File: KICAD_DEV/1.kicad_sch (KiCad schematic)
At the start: 0 parts

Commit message: wired my TMC2209 :D
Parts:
- added C18: 220uF, symbol Device:C
- added C19: 0.1uF, Capacitor_SMD:C_0805_2012Metric, symbol Device:C
- added C20: 0.1uF, symbol Device:C
- added J3, J4: Conn_01x08, symbol Connector_Generic:Conn_01x08
- added J5: Conn_01x02, symbol Connector_Generic:Conn_01x02
- added J6: Conn_01x04, symbol Connector_Generic:Conn_01x04
- added R10, R7, R8, R9: 10K, symbol Device:R
- added R5, R6: 1K, symbol Device:R
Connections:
- new net: J3.7 (Pin_7), R9.1
- new net: J3.5 (Pin_5), R7.1
- new net: J3.6 (Pin_6), R8.1
- new net: J4.3 (Pin_3), J6.4 (Pin_4)
- new net: J4.4 (Pin_4), J6.3 (Pin_3)
- new net: J4.5 (Pin_5), J6.2 (Pin_2)
- new net: J4.6 (Pin_6), J6.1 (Pin_1)
- new net: J3.4 (Pin_4), R5.1, R6.2
- new net +12V: C18.1, C19.1, J4.8 (Pin_8)
- new net +3V3: C20.1, J4.2 (Pin_2), R10.1
- new net GND: C18.2, C19.2, C20.2, J4.1 (Pin_1), J4.7 (Pin_7), R7.2, R8.2, R9.2
- new net TMC2209_DIAG: J5.1 (Pin_1)
- new net TMC2209_DIR: J3.1 (Pin_1)
- new net TMC2209_EN: J3.8 (Pin_8), R10.2
- new net TMC2209_INDEX: J5.2 (Pin_2)
- new net TMC2209_RX: R5.2
- new net TMC2209_STEP: J3.2 (Pin_2)
- new net TMC2209_TX: R6.1
- no-connect marks 0 -> 1
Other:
- note added: "TMC2209"

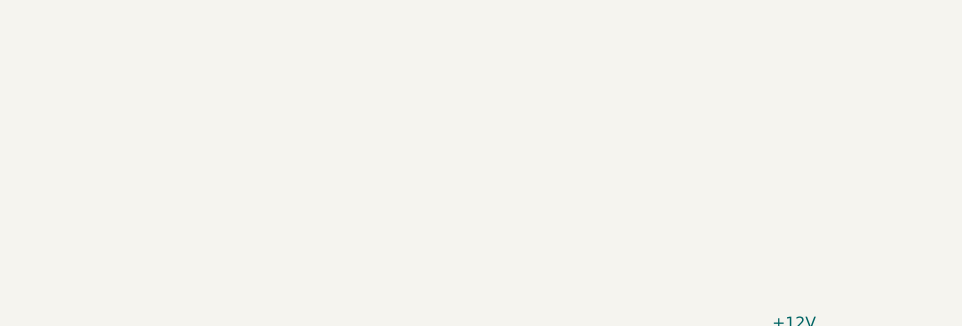
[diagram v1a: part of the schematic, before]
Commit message: layed out all the components
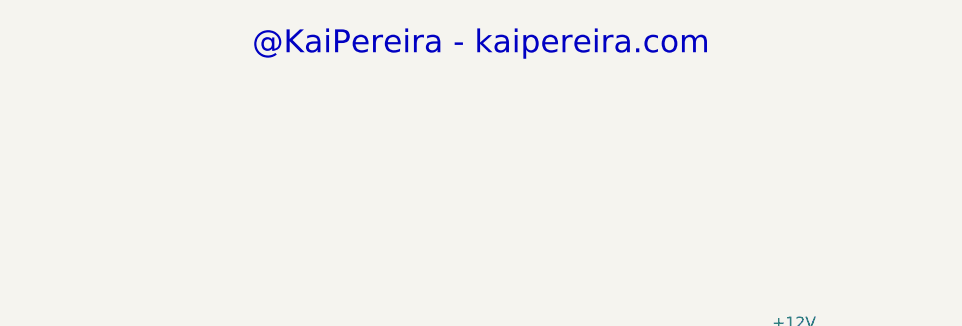
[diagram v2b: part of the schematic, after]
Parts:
- C18: footprint (none) -> Capacitor_SMD:C_Elec_8x6.2; Part (none) -> SPT1EM221F09TRVZC
- C20: footprint (none) -> Capacitor_SMD:C_0603_1608Metric
- J3, J4: footprint (none) -> Connector_PinSocket_2.54mm:PinSocket_1x08_P2.54mm_Vertical
- J5: footprint (none) -> Connector_PinSocket_2.54mm:PinSocket_1x02_P2.54mm_Vertical
- J6: footprint (none) -> Connector_JST:JST_XH_B4B-XH-AM_1x04_P2.50mm_Vertical
- R10, R5, R6, R7, R8, R9: footprint (none) -> Resistor_SMD:R_0402_1005Metric
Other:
- note added: "@KaiPereira - kaipereira.com"
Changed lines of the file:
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@@
 	(generator_version "9.0")
 	(paper "A3")
+	(text "@KaiPereira - kaipereira.com"
+		(exclude_from_sim no)
+		(at 182.372 45.212 0)
+		(effects
+			(font
+				(size 2.54 2.54)
+			)
+		)
+	)
 	(text "TMC2209"
 		(exclude_from_sim no)
@@
 			)
 		)
-		(property "Footprint" ""
+		(property "Footprint" "Resistor_SMD:R_0402_1005Metric"
 			(at 159.512 133.35 90)
 			(effects
@@
 			)
 		)
-		(property "Footprint" ""
+		(property "Footprint" "Resistor_SMD:R_0402_1005Metric"
 			(at 169.672 133.35 90)
 			(effects
@@
 			)
 		)
-		(property "Footprint" ""
+		(property "Footprint" "Resistor_SMD:R_0402_1005Metric"
 			(at 165.862 102.87 90)
 			(effects
@@
 			)
 		)
-		(property "Footprint" ""
+		(property "Footprint" "Resistor_SMD:R_0402_1005Metric"
 			(at 164.592 133.35 90)
 			(effects
@@
 			)
 		)
-		(property "Footprint" ""
+		(property "Footprint" "Connector_PinSocket_2.54mm:PinSocket_1x08_P2.54mm_Vertical"
 			(at 191.77 118.11 0)
 			(effects
@@
 			)
 		)
-		(property "Footprint" ""
+		(property "Footprint" "Resistor_SMD:R_0402_1005Metric"
 			(at 132.842 113.03 90)
 			(effects
@@
 			)
 		)
-		(property "Footprint" ""
+		(property "Footprint" "Capacitor_SMD:C_0603_1608Metric"
 			(at 239.7252 91.44 0)
 			(effects
@@
 			)
 		)
-		(property "Footprint" ""
+		(property "Footprint" "Connector_PinSocket_2.54mm:PinSocket_1x08_P2.54mm_Vertical"
 			(at 177.8 118.11 0)
 			(effects
@@
 			)
 		)
-		(property "Footprint" ""
+		(property "Footprint" "Connector_PinSocket_2.54mm:PinSocket_1x02_P2.54mm_Vertical"
 			(at 180.34 107.95 0)
 			(effects
@@
 			)
 		)
-		(property "Footprint" ""
+		(property "Footprint" "Resistor_SMD:R_0402_1005Metric"
 			(at 132.842 123.19 90)
 			(effects
@@
 			)
 		)
-		(property "Footprint" ""
+		(property "Footprint" "Capacitor_SMD:C_Elec_8x6.2"
 			(at 214.3252 91.44 0)
 			(effects
@@
 		)
 		(property "Description" "Unpolarized capacitor"
+			(at 213.36 87.63 0)
+			(effects
+				(font
+					(size 1.27 1.27)
+				)
+				(hide yes)
+			)
+		)
+		(property "Part" "SPT1EM221F09TRVZC"
 			(at 213.36 87.63 0)
 			(effects
@@
 			)
 		)
-		(property "Footprint" ""
+		(property "Footprint" "Connector_JST:JST_XH_B4B-XH-AM_1x04_P2.50mm_Vertical"
 			(at 217.17 115.57 0)
 			(effects
